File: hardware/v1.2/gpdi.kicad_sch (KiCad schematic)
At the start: 20 parts, among them J2 HDMI_C_1.3, U1 ECP5-CABGA256, U5 PCA9306DC1

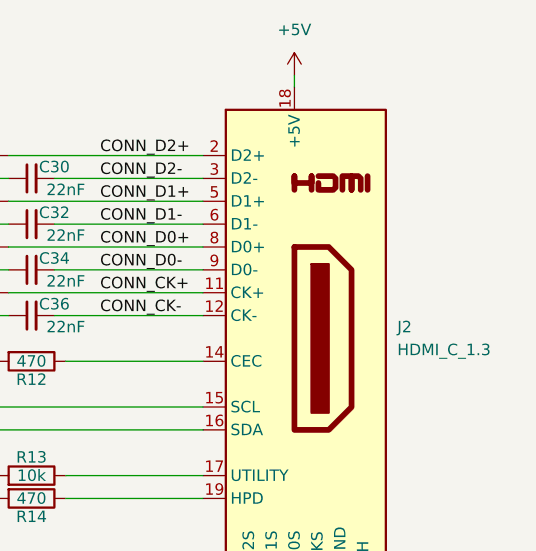
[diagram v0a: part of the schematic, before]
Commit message: Added start of documentation and changed GPDI
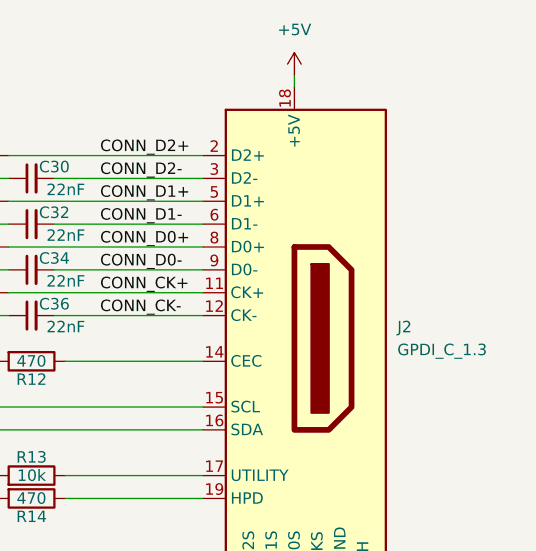
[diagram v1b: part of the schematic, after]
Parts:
- J2: value HDMI_C_1.3 -> GPDI_C_1.3; symbol Connector:HDMI_C_1.3 -> icepi-lib:GPDI_C_1.3; LCSC Link (none) -> https://lcsc.com/product-detail/HDMI-Connectors_XKB-Connect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; Manufactuer Part Number (none) -> A71-05H4-111N1
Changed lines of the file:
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@@
 	)
 	(symbol
-		(lib_id "Connector:HDMI_C_1.3")
+		(lib_id "icepi-lib:GPDI_C_1.3")
 		(at 196.85 77.47 0)
 		(unit 1)
@@
 			)
 		)
-		(property "Value" "HDMI_C_1.3"
+		(property "Value" "GPDI_C_1.3"
 			(at 208.28 78.7399 0)
 			(effects
@@
 			)
 		)
-		(property "Datasheet" "http://pinoutguide.com/PortableDevices/mini_hdmi_pinout.shtml"
+		(property "Datasheet" "-"
 			(at 197.485 77.47 0)
 			(effects
@@
 			)
 		)
-		(property "Description" "HDMI 1.3+ type C connector"
+		(property "Description" "GPDI type C connector"
 			(at 196.85 77.47 0)
 			(effects
@@
 			(at 196.85 77.47 0)
 			(effects
+				(font
+					(size 1.27 1.27)
+				)
+				(hide yes)
+			)
+		)
+		(property "LCSC Link" "https://lcsc.com/product-detail/HDMI-Connectors_XKB-Connection-A71-05H4-111N1_C2682170.html"
+			(at 196.85 77.47 0)
+			(effects
+				(font
+					(size 1.27 1.27)
+				)
+				(hide yes)
+			)
+		)
+		(property "Manufactuer Part Number" "A71-05H4-111N1"
+			(at 196.85 77.47 0)
+			(effects
